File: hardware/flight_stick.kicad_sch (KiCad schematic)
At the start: 22 parts, among them J10 USB_C_Receptacle_USB2.0, J9 Conn_ST_STDC14, SW1 KMR223G LFG, U4 STM32F103CBU6, Y1 8M

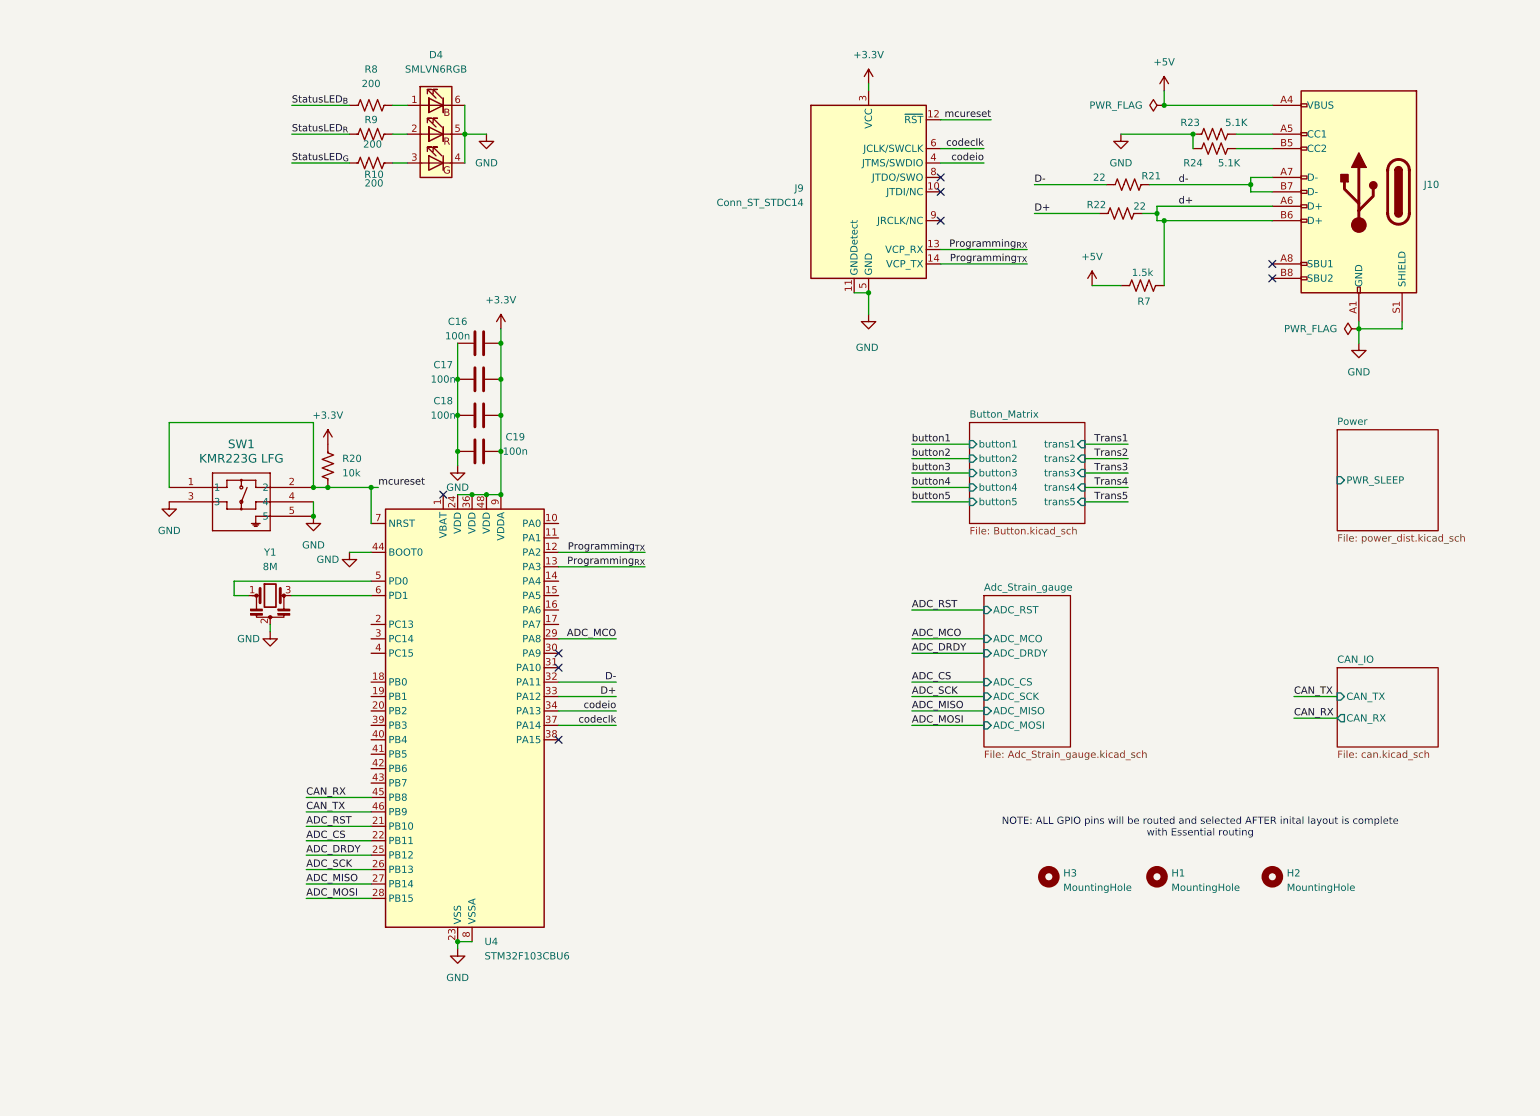
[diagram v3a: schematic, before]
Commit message: Added EEPROM, resolved comments
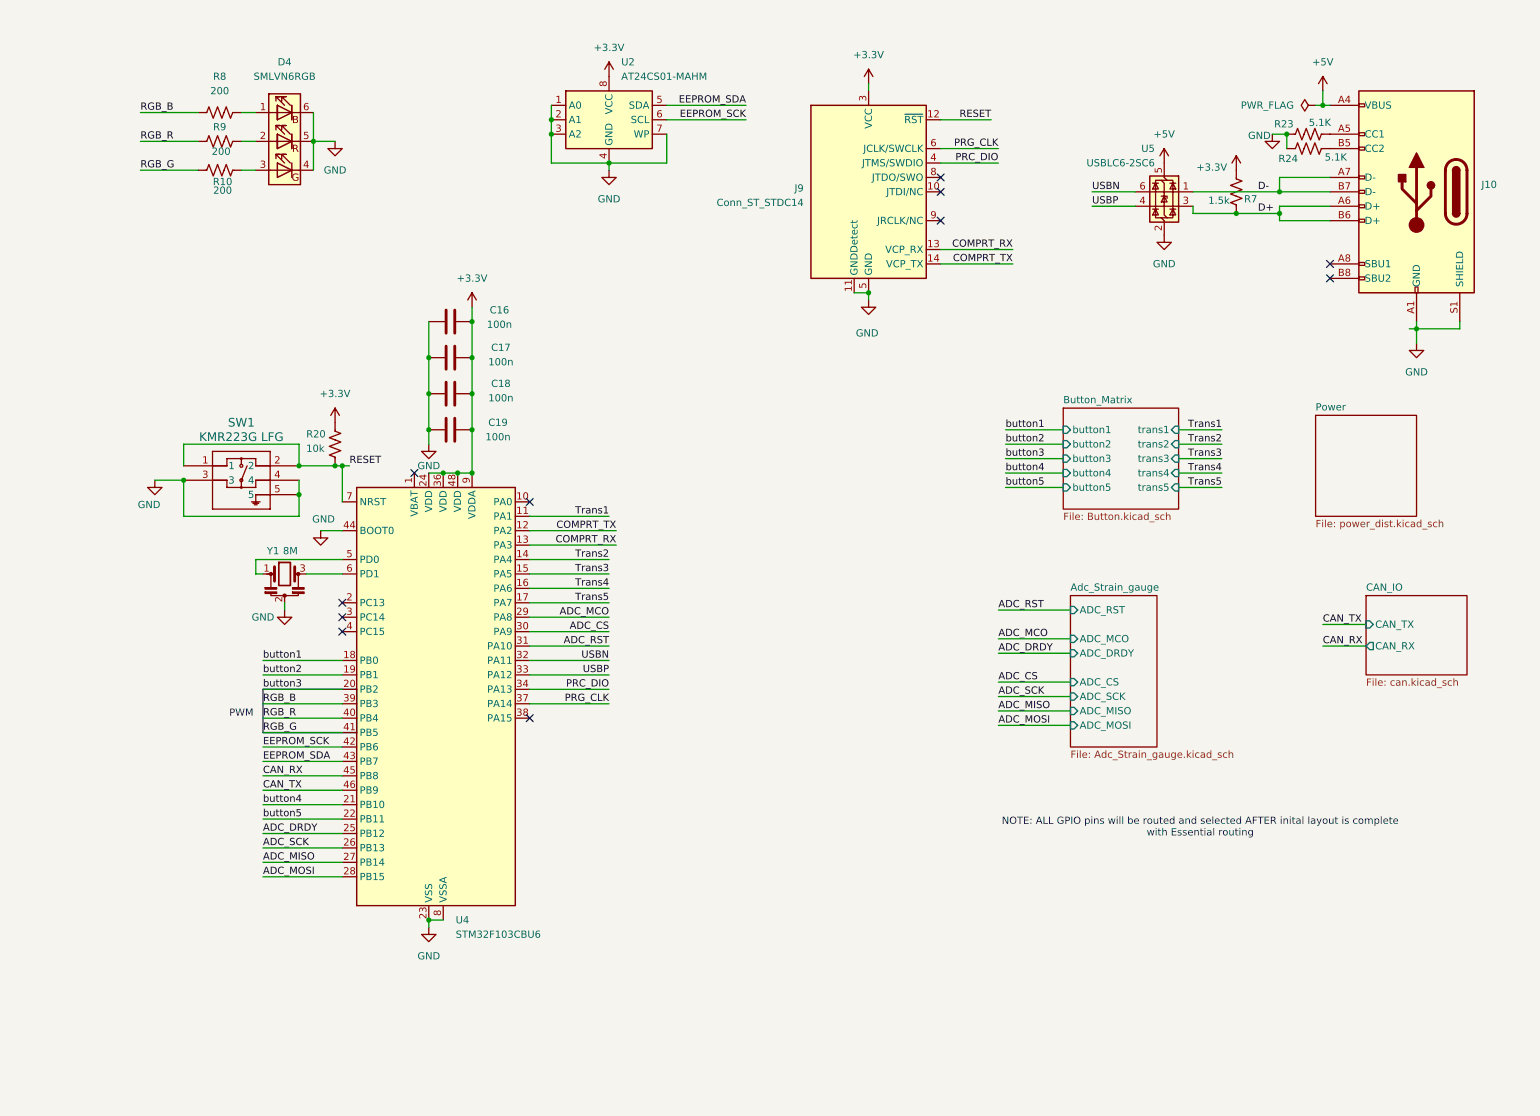
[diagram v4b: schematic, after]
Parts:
- removed H1, H2, H3: MountingHole, MountingHole:MountingHole_3.2mm_M3_ISO7380, symbol Mechanical:MountingHole
- removed R21, R22: 22, Resistor_SMD:R_0603_1608Metric, symbol Device:R_US
- added U2: AT24CS01-MAHM, Package_DFN_QFN:DFN-8-1EP_3x2mm_P0.5mm_EP1.3x1.5mm, symbol Memory_EEPROM:AT24CS01-MAHM
- added U5: USBLC6-2SC6, Package_TO_SOT_SMD:SOT-23-6, symbol Power_Protection:USBLC6-2SC6
- SW1: footprint flight_stick_footprints:KMR2_G_CNK -> KMR2_G_CNK
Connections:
- net StatusLED_{B} is gone; now on net RGB_B: R8.1
- net StatusLED_{G} is gone; now on net RGB_G: R10.1
- net StatusLED_{R} is gone; now on net RGB_R: R9.1
- net d- is gone; now on net D-: J10.A7 (D-), J10.B7 (D-)
- net +3.3V: now also R7.1, U2.8 (VCC)
- net +5V: now also U5.5 (VBUS); no longer R7.2
- net ADC_CS: now also U4.30 (PA9); no longer U4.22 (PB11)
- net ADC_RST: now also U4.31 (PA10); no longer U4.21 (PB10)
- net D+: now also J10.A6 (D+), J10.B6 (D+), R7.2, U5.3 (I/O2); no longer U4.33 (PA12)
- net D-: now also U5.1 (I/O1); no longer U4.32 (PA11)
- net GND: now also U2.1 (A0), U2.2 (A1), U2.3 (A2), U2.4 (GND), U2.7 (WP), U2.9 (GND), U5.2 (GND)
- net Trans1: now also U4.11 (PA1)
- net Trans2: now also U4.14 (PA4)
- net Trans3: now also U4.15 (PA5)
- net Trans4: now also U4.16 (PA6)
- net Trans5: now also U4.17 (PA7)
- net button1: now also U4.18 (PB0)
- net button2: now also U4.19 (PB1)
- net button3: now also U4.20 (PB2)
- net button4: now also U4.21 (PB10)
- net button5: now also U4.22 (PB11)
- net RGB_B: now reaches U4.39 (PB3)
- net RGB_R: now reaches U4.40 (PB4)
- net RGB_G: now reaches U4.41 (PB5)
- net EEPROM_SCK: now reaches U4.42 (PB6)
- net EEPROM_SCK: now also U2.6 (SCL)
- net EEPROM_SDA: now reaches U4.43 (PB7)
- net EEPROM_SDA: now also U2.5 (SDA)
- net Programming_{RX} renamed COMPRT_RX
- net Programming_{TX} renamed COMPRT_TX
- net codeclk renamed PRG_CLK
- net codeio renamed PRC_DIO
- removed net d+: J10.A6 (D+), J10.B6 (D+), R7.1
- net mcureset renamed RESET
- new net USBN: U4.32 (PA11), U5.6 (I/O1)
- new net USBP: U4.33 (PA12), U5.4 (I/O2)
- no-connect marks 9 -> 11
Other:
- sheet Power ports: added none; removed PWR_SLEEP
- note added: "PWM"
- company: Aryan Ghosh -> University of Toronto Human Powered Vehicles
- title: Flight Stick -> Master 
- moved on the sheet: C16, C17, C18, C19, D4, J10, R10, R20, R23, R24, R7, R8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

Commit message: Stylistic changes
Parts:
- added R2, R3: 4.7k, Resistor_SMD:R_0603_1608Metric, symbol Device:R_US
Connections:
- net +3.3V: now also R2.1, R3.1
- net EEPROM_SCK: now also R2.2
- net EEPROM_SDA: now also R3.2
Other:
- moved on the sheet: D4, R10, R8, R9, U2

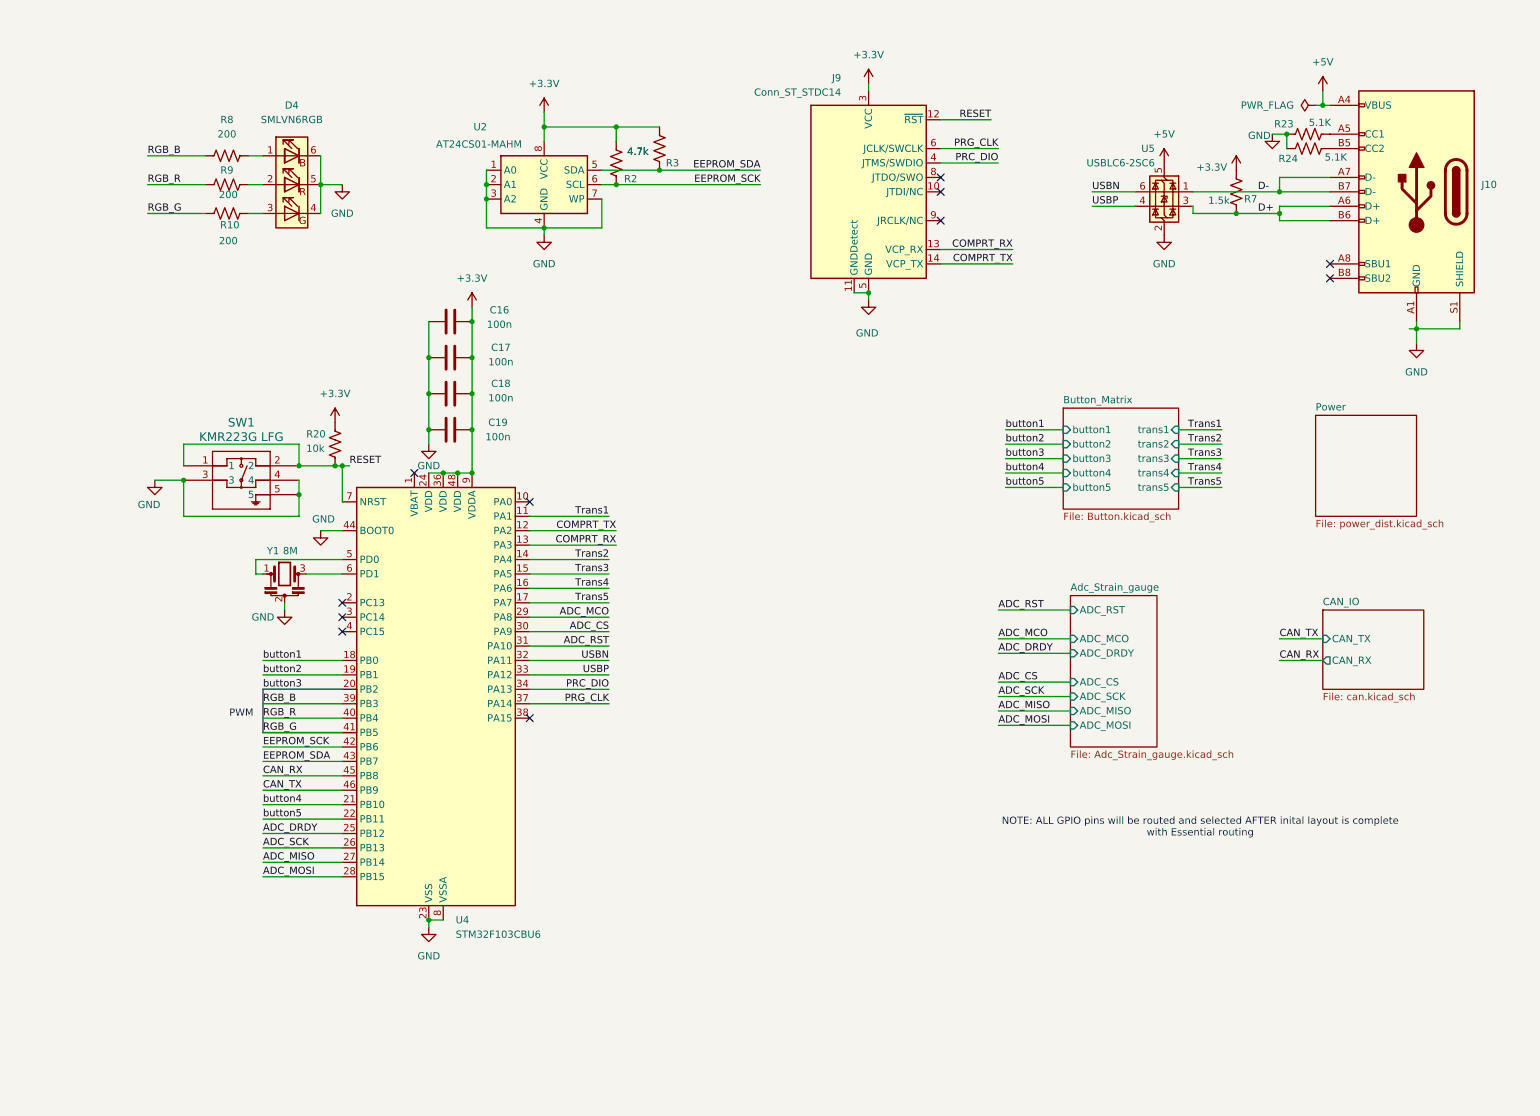
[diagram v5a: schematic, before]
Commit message: revamped button matrix
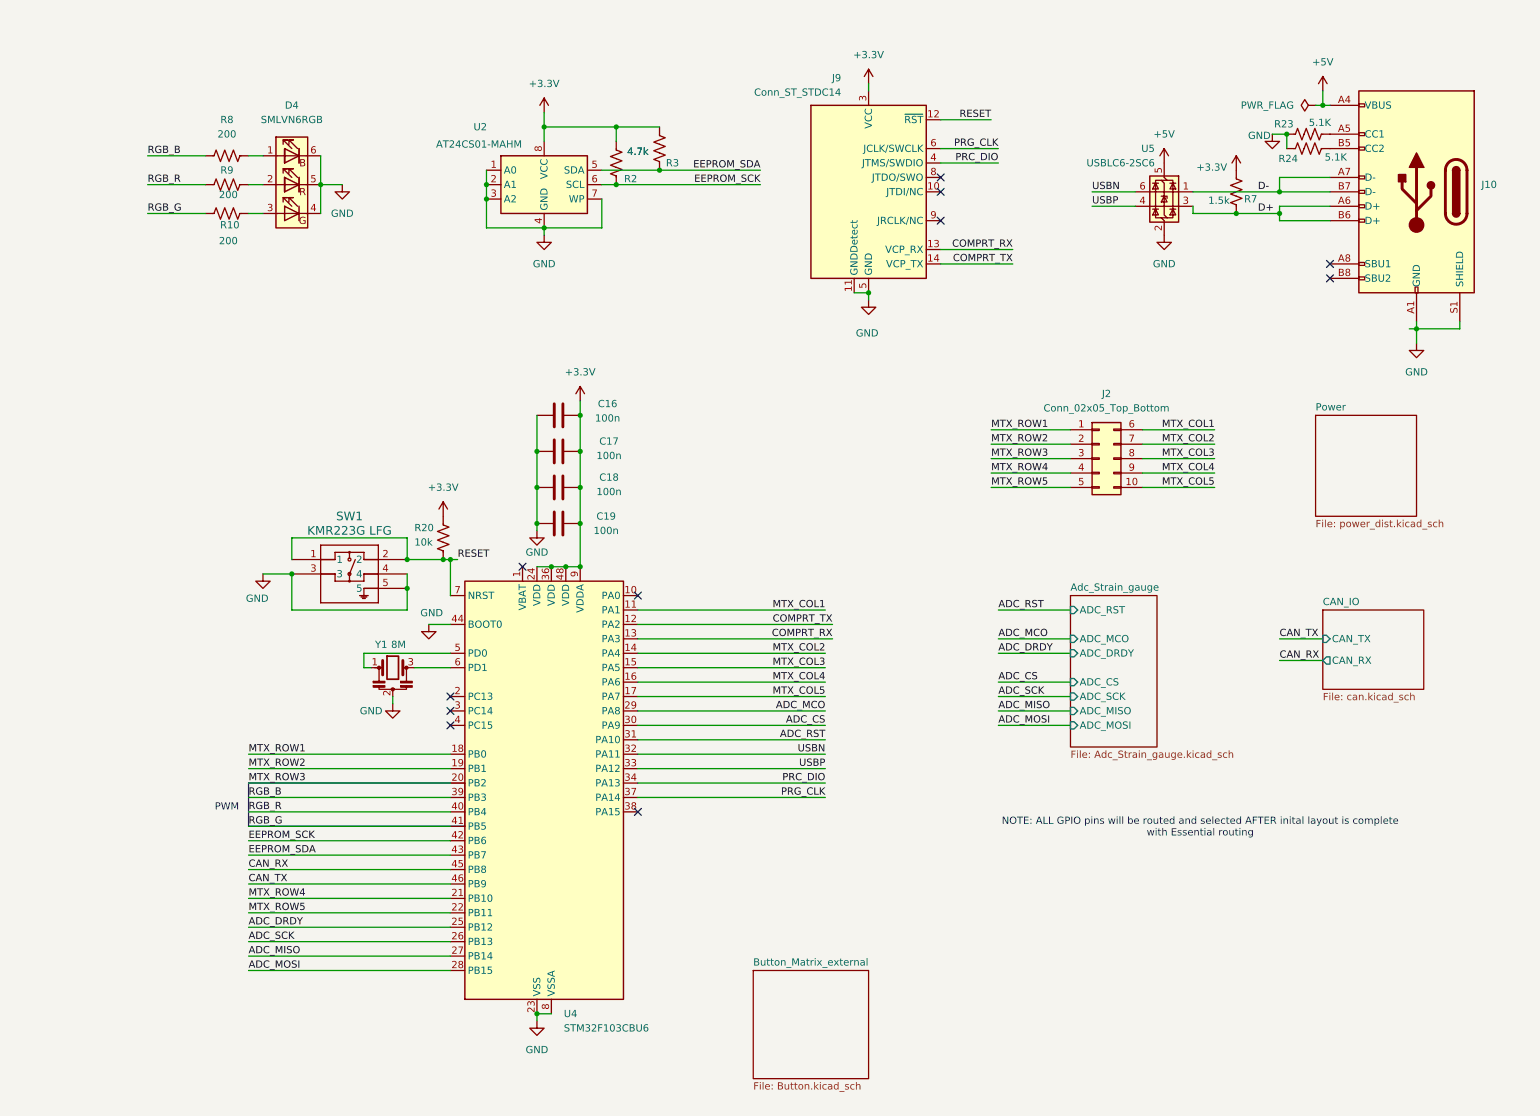
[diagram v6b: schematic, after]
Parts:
- added J2: Conn_02x05_Top_Bottom, symbol Connector_Generic:Conn_02x05_Top_Bottom
- SW1: footprint KMR2_G_CNK -> flight_stick_footprints:KMR2_G_CNK
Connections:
- net Trans1 renamed MTX_COL1
- net MTX_COL1: now also J2.6 (Pin_6)
- net Trans2 renamed MTX_COL2
- net MTX_COL2: now also J2.7 (Pin_7)
- net Trans3 renamed MTX_COL3
- net MTX_COL3: now also J2.8 (Pin_8)
- net Trans4 renamed MTX_COL4
- net MTX_COL4: now also J2.9 (Pin_9)
- net Trans5 renamed MTX_COL5
- net MTX_COL5: now also J2.10 (Pin_10)
- net button1 renamed MTX_ROW1
- net MTX_ROW1: now also J2.1 (Pin_1)
- net button2 renamed MTX_ROW2
- net MTX_ROW2: now also J2.2 (Pin_2)
- net button3 renamed MTX_ROW3
- net MTX_ROW3: now also J2.3 (Pin_3)
- net button4 renamed MTX_ROW4
- net MTX_ROW4: now also J2.4 (Pin_4)
- net button5 renamed MTX_ROW5
- net MTX_ROW5: now also J2.5 (Pin_5)
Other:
- sheet Button_Matrix renamed Button_Matrix_external
- sheet Button_Matrix_external ports: added none; removed button1, button2, button3, button4, button5, trans1, trans2, trans3, trans4, trans5
- moved on the sheet: C16, C17, C18, C19, R20, SW1, U4, Y1

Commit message: Finished footprint assignment and deleted pcb
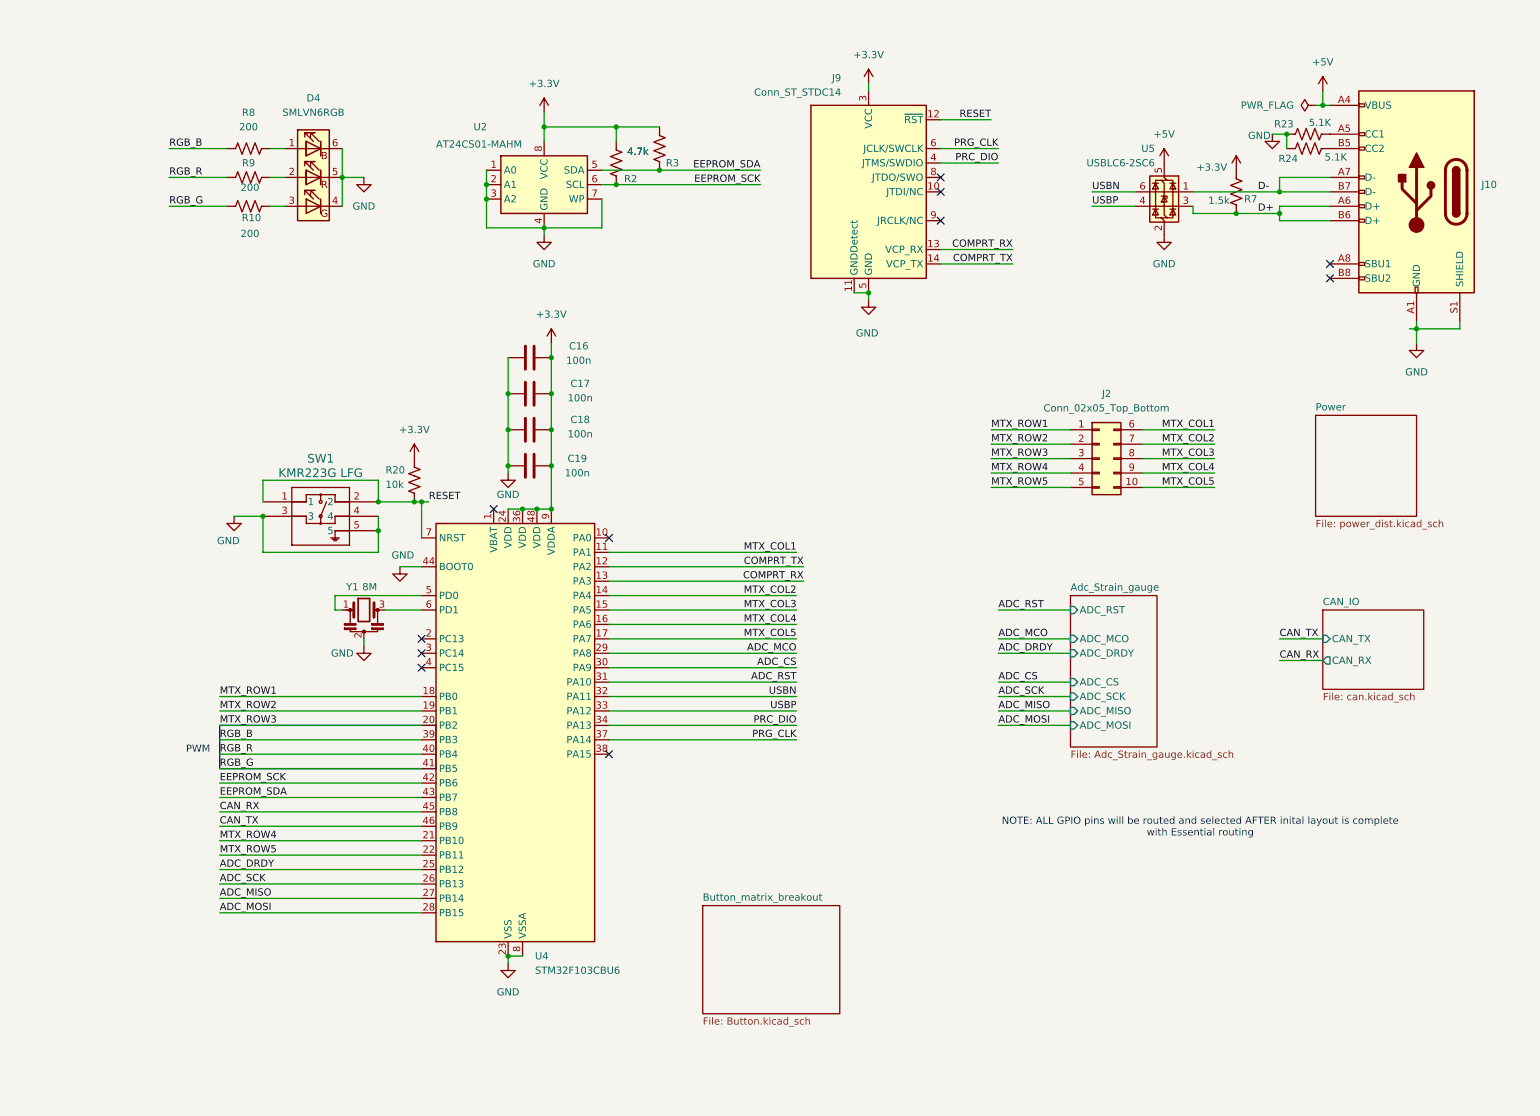
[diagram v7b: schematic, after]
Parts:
- J2: footprint (none) -> Connector_JST:JST_J2100_B10B-J21DK-GGXR_2x05_P2.50x4.00mm_Vertical
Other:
- sheet Button_Matrix_external renamed Button_matrix_breakout
- moved on the sheet: C16, C17, C18, C19, D4, R10, R20, R8, R9, SW1, U4, Y1
